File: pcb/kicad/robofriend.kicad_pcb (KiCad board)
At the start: 2 copper layers, 125 parts, among them J1 PWR, J10 US1, J11 12V-Buck, J12 12V-Buck-Boost, J13 5VIN, J14 5VOUT, J15 5VOUT, J16 US2, J17 US3, J18 USB_A_4_PIN, J19 US4, J2 PWR, J20 12V-Reg, J21 MON/AMP, J22 ADC1, J23 MRi, J24 SPI, J25 ADC2, J26 MLe, J27 M1, J28 M2, J29 IR1, J3 3V3OUT, J30 IR2, J31 UART, J32 IR3, J33 GS2, J34 UART, J4 3V3OUT, J5 GS2, J6 I2C, J7 I2C, J8 I2C, J9 I2C, K1 SCHRACK-RTx3, Q1 NMOS, Q2 NMOS, Q3 NMOS, Q4 NPN, Q5 PMOS, Q6 NMOS, Q7 NMOS, U1 LM3940-3.3, U2 Teensy++2.0, U3 TL331, U4 LM4040, U5 MCP6001, U6 INA193, U7 TL331, U8 TXS0102

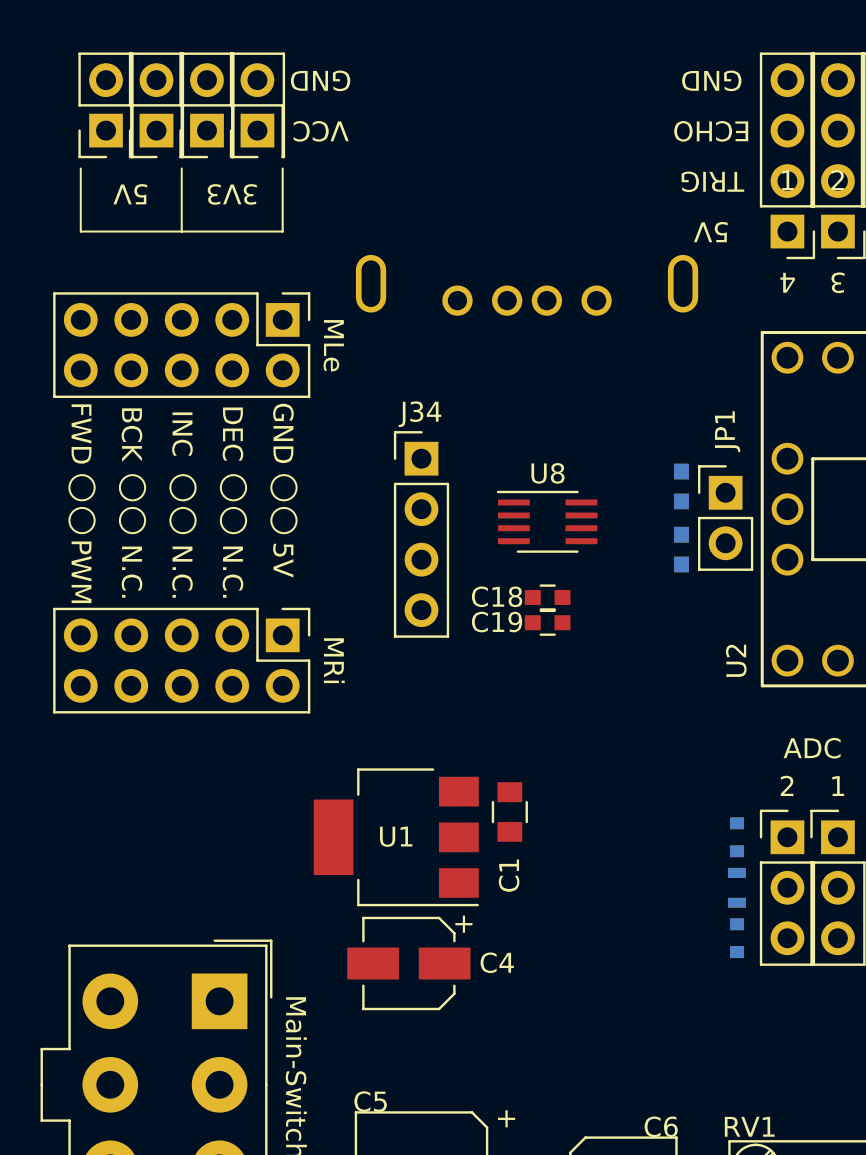
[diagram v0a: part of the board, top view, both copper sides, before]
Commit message: added PCA9517 for i2c level shifting
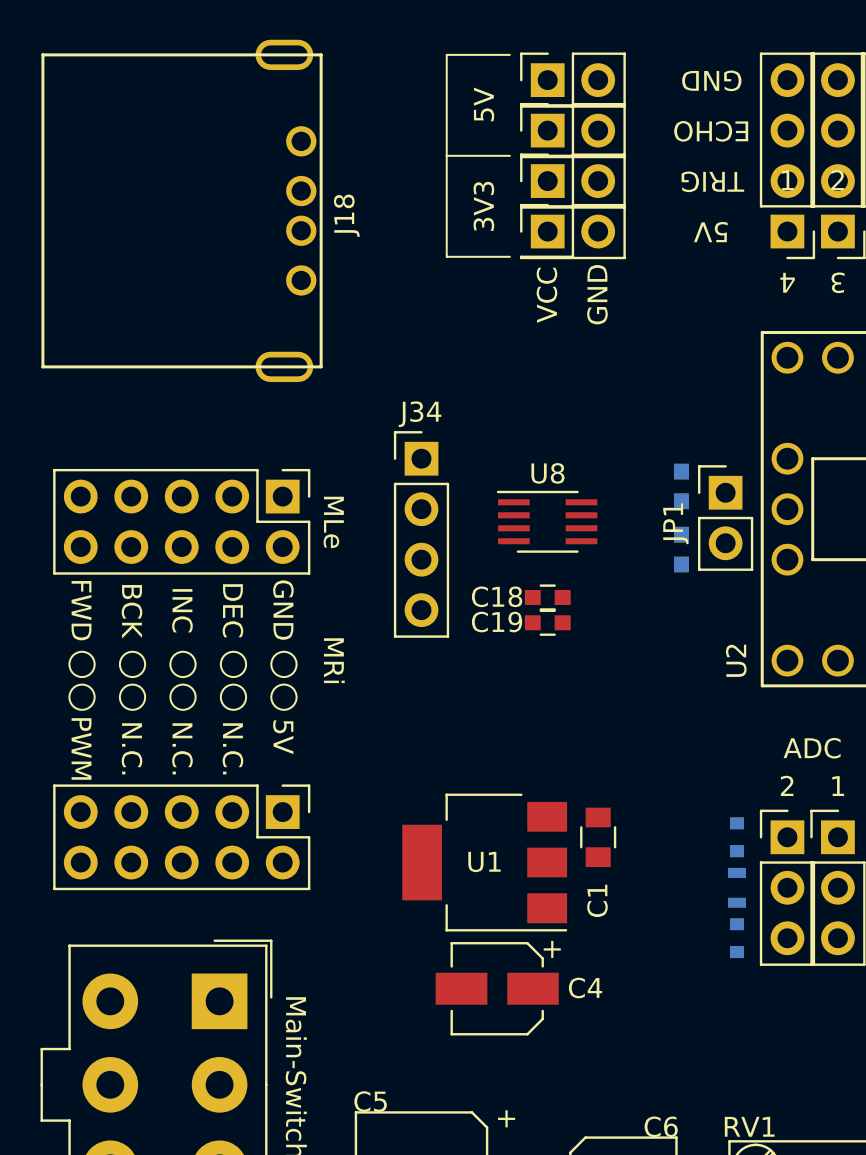
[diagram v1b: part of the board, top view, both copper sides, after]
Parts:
- J18: moved to F.Cu
- moved J15 22.4 mm to (108.6, 71.1), turned to 0 degrees
- moved J14 19.7 mm to (108.6, 73.7), turned to 0 degrees
- moved J4 17.3 mm to (108.6, 76.2), turned to 0 degrees
- moved J18 16.5 mm to (83.2, 69.8), turned to 270 degrees
- moved J3 15.5 mm to (108.6, 78.7), turned to 0 degrees
- moved J23 8.89 mm to (95.2, 108.0)
- moved J26 8.89 mm to (95.2, 92.1)
- moved C4 4.62 mm to (106.0, 116.8)
- moved C1 4.62 mm to (111.1, 109.2)
- moved U1 4.62 mm to (105.4, 110.5)

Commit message: layout complete, starting to route
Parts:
- removed the C18 at (108.6, 97.2)
- removed the C19 at (108.6, 98.4)
- removed J34: UART, Pin_Headers:Pin_Header_Straight_1x04_Pitch2.54mm
- removed JP5: Jumper, Pin_Headers:Pin_Header_Straight_1x03_Pitch2.54mm
- removed the Q2 at (156.2, 77.5)
- removed the Q3 at (156.2, 73.0)
- removed Q6, Q7: NMOS, TO_SOT_Packages_SMD:SOT-23
- removed the R27 at (146.7, 76.2)
- removed R28, R30, R31: 10k, Resistors_SMD:R_0603
- removed the U8 at (108.6, 93.3)
- added C13: 100n, Capacitors_SMD:C_0603, B.Cu at (148.0, 73.0)
- added C14: 100n, Capacitors_SMD:C_0603, B.Cu at (148.0, 76.8)
- added U4: PCA9517, Housings_SOIC:SOIC-8_3.9x4.9mm_Pitch1.27mm, F.Cu at (151.8, 74.9)
- C1: moved to B.Cu
- moved C10 13.7 mm to (133.7, 121.6), turned to 270 degrees
- moved C9 9.85 mm to (135.6, 121.6), turned to 270 degrees
- moved R8 8.47 mm to (150.5, 74.3), turned to 180 degrees
- moved J22 8.26 mm to (135.9, 78.7)
- moved C1 7.99 mm to (103.2, 108.3), turned to 0 degrees
- moved JP2 7.62 mm to (143.5, 77.5)
- moved J15 7.43 mm to (101.6, 73.7), turned to 90 degrees
- moved R11 7.01 mm to (153.0, 80.0), turned to 180 degrees
- moved C4 6.30 mm to (110.8, 112.7), turned to 270 degrees
- moved R7 6.25 mm to (153.0, 74.3), turned to 0 degrees
- moved C7 6.04 mm to (137.5, 121.6), turned to 270 degrees
- moved J3 5.12 mm to (109.2, 73.7), turned to 90 degrees
- moved C11 4.49 mm to (135.3, 124.5)
- moved J14 4.44 mm to (104.1, 73.7), turned to 90 degrees
- moved C12 4.42 mm to (146.1, 123.8)
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- renumbered C13 to C15, C14 to C16, C15 to C17, C16 to C18, C17 to C19, D13 to D10, D5 to D11, D6 to D12, D15 to D13, D16 to D14, D7 to D15, D8 to D16, D9 to D5, D10 to D6, D11 to D7, D14 to D8, D12 to D9, J31 to J22, J26 to J25, J27 to J26, J28 to J27, J29 to J28, J22 to J29, J25 to J31, Q4 to Q2, Q5 to Q3, R13 to R12, R14 to R13, R15 to R14, R16 to R15, R17 to R16, R18 to R17, R20 to R18, R21 to R19, R22 to R20, R24 to R21, R25 to R22, R12 to R24, R26 to R25, R19 to R26, R29 to R27, U4 to U5, U5 to U6, U6 to U7, U7 to U8
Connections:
- J22 pad 1: Net-(J31-Pad1) -> +5V
- J22 pad 2: Net-(J31-Pad2) (its old number) -> D2
- J22 pad 3: Net-(J31-Pad3) -> D3
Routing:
- net Net-(C6-Pad1): track 1.61 -> 0.00 mm
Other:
- board text added: "U4"
- board text removed: "UART"

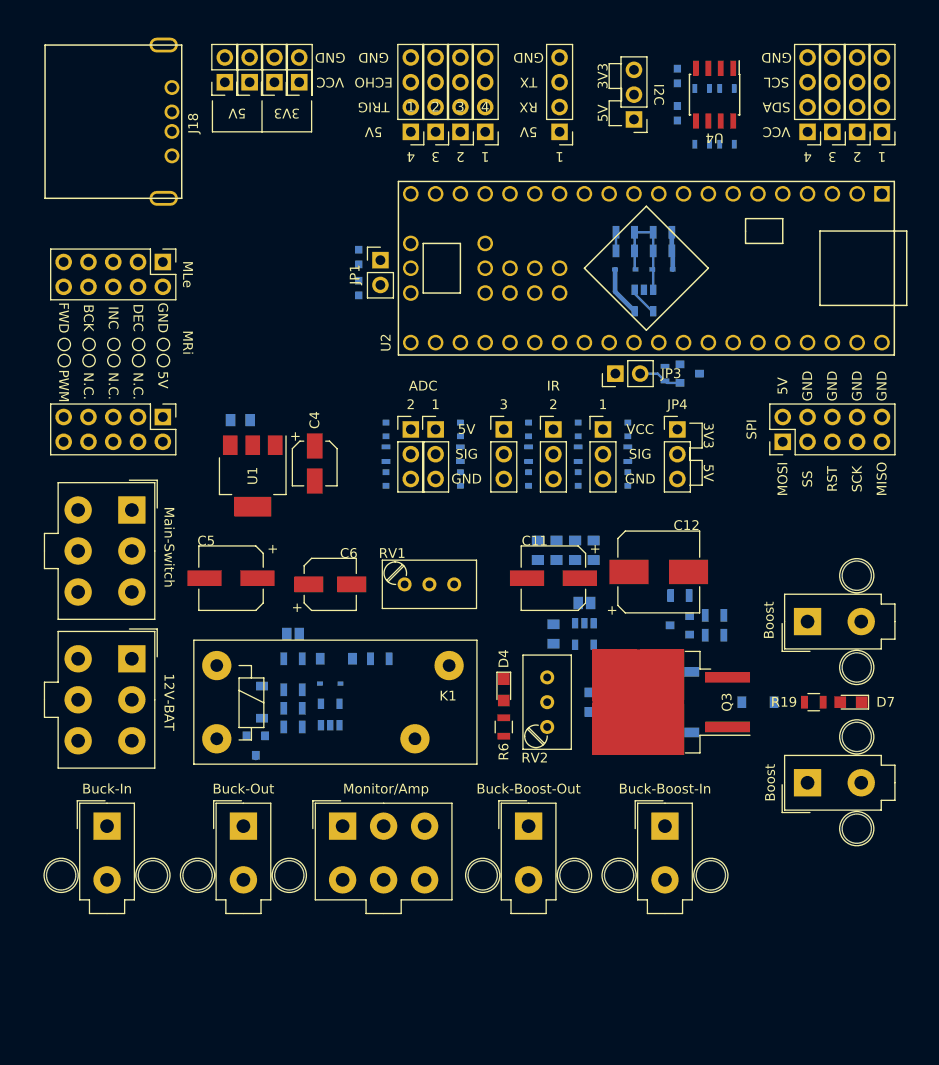
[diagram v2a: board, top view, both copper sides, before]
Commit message: added 74lvc1t45 to schmatic (uart lvl shift), completed the schmeatic by doing last beautification
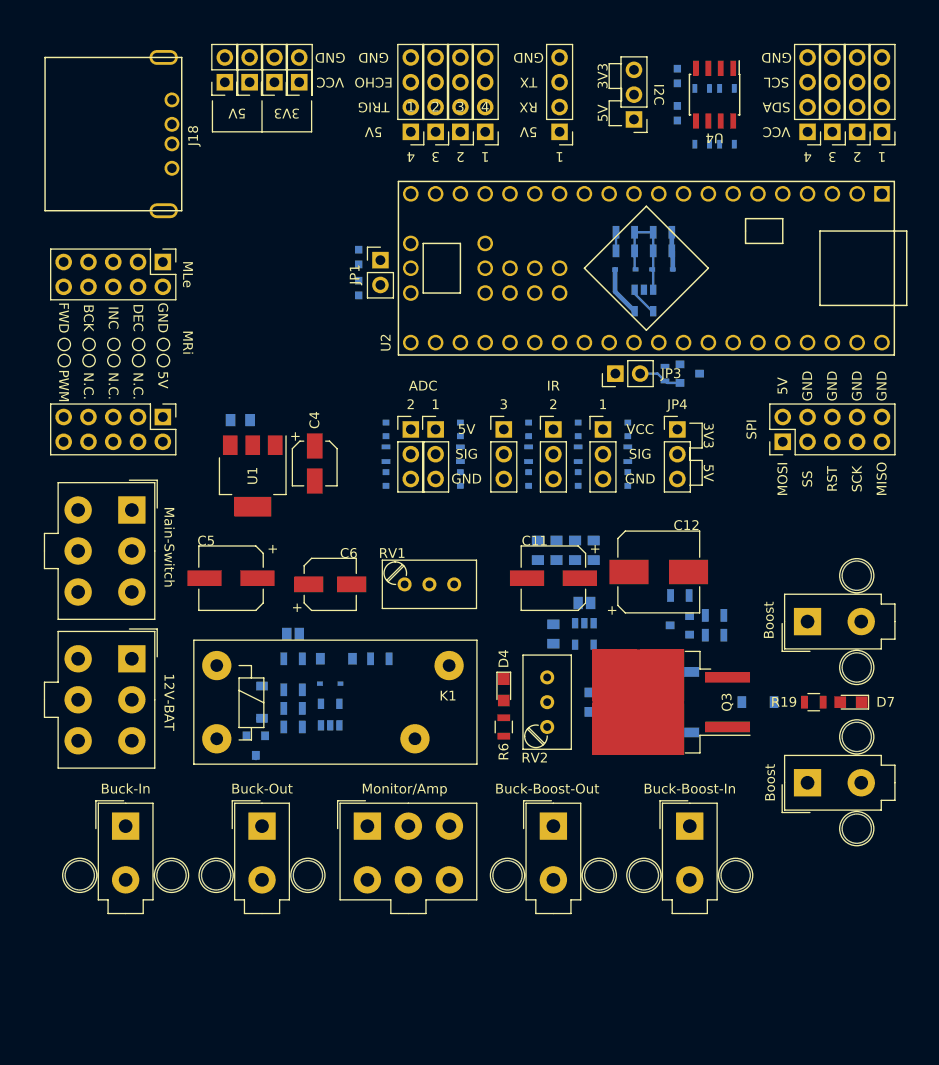
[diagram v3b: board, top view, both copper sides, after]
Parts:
- moved J12 2.54 mm to (135.3, 149.9)
- moved J20 2.54 mm to (149.2, 149.9)
- moved J21 2.54 mm to (116.2, 149.9)
- moved J11 1.91 mm to (105.4, 149.9)
- moved J13 1.91 mm to (91.4, 149.9)
- moved J18 1.27 mm to (83.2, 71.1)
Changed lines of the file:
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@@
   )
   (module Connectors_Molex:Molex_MiniFit-JR-5556-02B_2x01x4.20mm_Straight (layer F.Cu)
-    (at 103.505 149.86)
+    (at 105.41 149.86)
     (descr "Molex Mini-Fit JR, PN:5556-02B, dual row, top entry type, through hole, with plastic PCB locators")
     (tags "connector molex mini-fit 5556")
@@
   )
   (module Connectors_Molex:Molex_MiniFit-JR-5556-02B_2x01x4.20mm_Straight (layer F.Cu)
-    (at 89.535 149.86)
+    (at 91.44 149.86)
     (descr "Molex Mini-Fit JR, PN:5556-02B, dual row, top entry type, through hole, with plastic PCB locators")
     (tags "connector molex mini-fit 5556")
@@
   )
   (module Connectors_Molex:Molex_MiniFit-JR-5556-06A_2x03x4.20mm_Straight (layer F.Cu)
-    (at 113.665 149.86)
+    (at 116.205 149.86)
     (descr "Molex Mini-Fit JR, PN:5556-06A, dual row, top entry type, through hole")
     (tags "connector molex mini-fit 5556")
@@
   )
   (module USB_A_4_PIN:MOLEX_48258_0001 (layer F.Cu)
-    (at 83.185 69.85 270)
+    (at 83.185 71.12 270)
     (descr "USB A connector")
     (tags "USB USB_A")
@@
   )
   (module Connectors_Molex:Molex_MiniFit-JR-5556-02B_2x01x4.20mm_Straight (layer F.Cu)
-    (at 132.715 149.86)
+    (at 135.255 149.86)
     (descr "Molex Mini-Fit JR, PN:5556-02B, dual row, top entry type, through hole, with plastic PCB locators")
     (tags "connector molex mini-fit 5556")
@@
   )
   (module Connectors_Molex:Molex_MiniFit-JR-5556-02B_2x01x4.20mm_Straight (layer F.Cu)
-    (at 146.685 149.86)
+    (at 149.225 149.86)
     (descr "Molex Mini-Fit JR, PN:5556-02B, dual row, top entry type, through hole, with plastic PCB locators")
     (tags "connector molex mini-fit 5556")
@@
     (effects (font (size 1 1) (thickness 0.15)))
   )
-  (gr_text Buck-Boost-In (at 146.685 146.05) (layer F.SilkS)
+  (gr_text Buck-Boost-In (at 149.225 146.05) (layer F.SilkS)
     (effects (font (size 1 1) (thickness 0.15)))
   )
-  (gr_text Buck-Boost-Out (at 132.715 146.05) (layer F.SilkS)
+  (gr_text Buck-Boost-Out (at 134.62 146.05) (layer F.SilkS)
     (effects (font (size 1 1) (thickness 0.15)))
   )
@@
     (effects (font (size 1 1) (thickness 0.15)))
   )
-  (gr_text Buck-In (at 89.535 146.05) (layer F.SilkS)
+  (gr_text Buck-In (at 91.44 146.05) (layer F.SilkS)
     (effects (font (size 1 1) (thickness 0.15)))
   )
-  (gr_text Buck-Out (at 103.505 146.05) (layer F.SilkS)
+  (gr_text Buck-Out (at 105.41 146.05) (layer F.SilkS)
     (effects (font (size 1 1) (thickness 0.15)))
   )
-  (gr_text Monitor/Amp (at 118.11 146.05) (layer F.SilkS)
+  (gr_text Monitor/Amp (at 120.015 146.05) (layer F.SilkS)
     (effects (font (size 1 1) (thickness 0.15)))
   )

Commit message: added 74lvc1t45 to layout (uart lvl shift), completed the layout, now starting to route
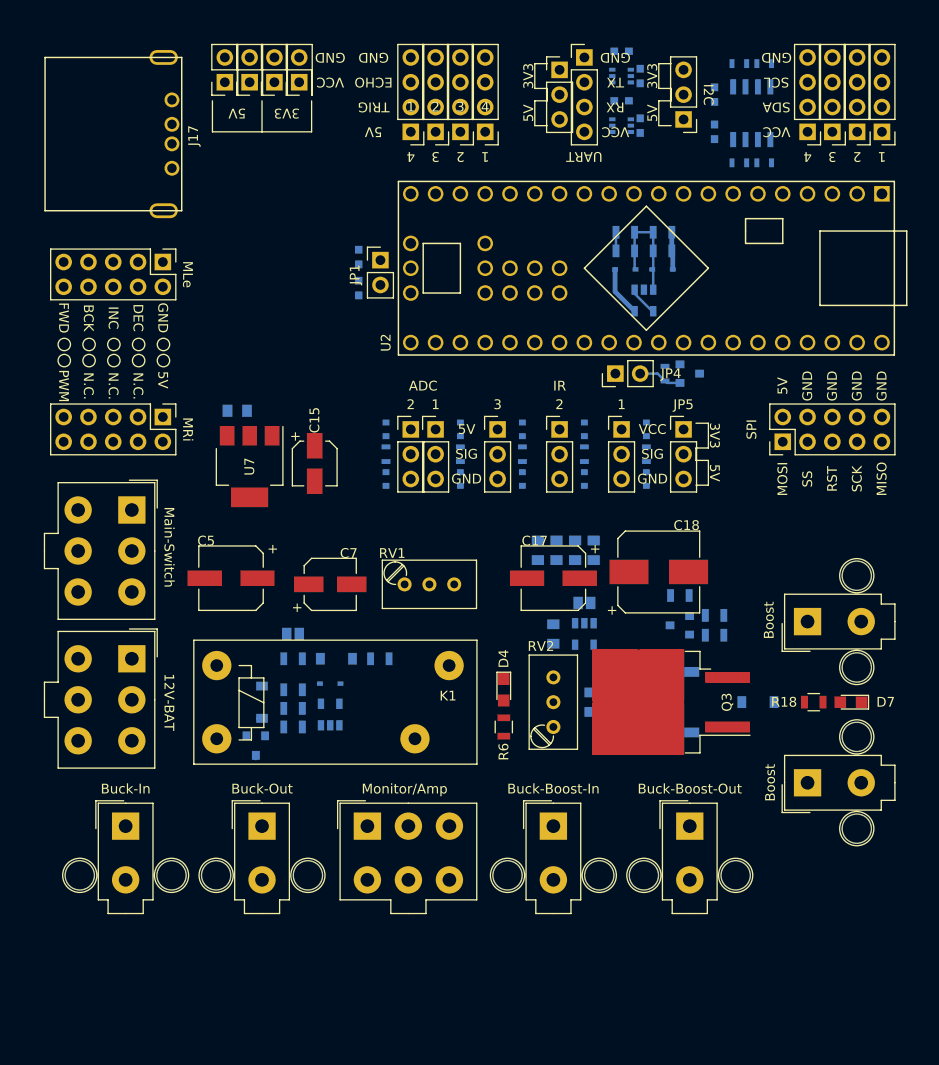
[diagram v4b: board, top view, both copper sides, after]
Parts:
- removed the J22 at (135.9, 78.7)
- added C3: 100n, Capacitors_SMD:C_0603, B.Cu at (142.2, 70.5)
- added C4: 100n, Capacitors_SMD:C_0603, B.Cu at (144.1, 73.0)
- added C6: 100n, Capacitors_SMD:C_0603, B.Cu at (142.2, 75.6)
- added C8: 100n, Capacitors_SMD:C_0603, B.Cu at (144.1, 78.1)
- added J1: UART, Pin_Headers:Pin_Header_Straight_1x04_Pitch2.54mm, F.Cu at (138.4, 71.1)
- added JP2: Jumper, Pin_Headers:Pin_Header_Straight_1x03_Pitch2.54mm, F.Cu at (135.9, 72.4)
- added U1: 74LVC1T45, TO_SOT_Packages_SMD:SOT-363_SC-70-6, B.Cu at (142.2, 73.0)
- added U4: 74LVC1T45, TO_SOT_Packages_SMD:SOT-363_SC-70-6, B.Cu at (142.2, 78.1)
- U5: renamed from U4; moved to B.Cu
- moved J11 14.0 mm to (149.2, 149.9)
- moved J18 14.0 mm to (135.3, 149.9)
- moved JP3 5.08 mm to (148.6, 77.5)
- moved R10 4.58 mm to (156.8, 71.8)
- moved R12 4.58 mm to (154.3, 71.8)
- moved R13 4.26 mm to (154.3, 81.9)
- moved R14 4.26 mm to (156.8, 81.9)
- moved U5 4.26 mm to (155.6, 76.8), turned to 90 degrees
- moved C10 4.26 mm to (151.8, 78.7)
- moved C9 4.26 mm to (151.8, 74.9)
- moved D10 1.91 mm to (144.8, 114.3)
- moved D9 1.91 mm to (144.8, 109.2)
- moved J28 1.91 mm to (142.2, 109.2)
- moved R22 1.91 mm to (144.8, 111.8)
- moved C11 1.00 mm to (102.9, 107.3)
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- renumbered C2 to C1, C14 to C10, C1 to C11, C7 to C12, C8 to C13, C9 to C14, C4 to C15, C10 to C16, C11 to C17, C12 to C18, C15 to C19, C3 to C2, C16 to C20, C17 to C21, C18 to C22, C19 to C23, C6 to C7, C13 to C9, J11 to J10, J12 to J11, J13 to J12, J14 to J13, J15 to J14, J16 to J15, J17 to J16, J18 to J17, J20 to J18, J21 to J19, J1 to J2, J19 to J20, J23 to J21, J24 to J22, J25 to J23, J3 to J24, J4 to J25, J2 to J3, J5 to J4, J6 to J5, J7 to J6, J8 to J7, J9 to J8, J10 to J9, JP2 to JP3, JP3 to JP4, JP4 to JP5, R7 to R10, R17 to R11, R8 to R12, R10 to R13, R11 to R14, R14 to R15, R18 to R17, R19 to R18, R20 to R19, R21 to R20, R22 to R21, R23 to R22, R9 to R23, R12 to R7, R13 to R8, R15 to R9, U8 to U10, U1 to U7, U5 to U8, U7 to U9
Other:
- board text added: "UART"
- board text removed: "U4"
